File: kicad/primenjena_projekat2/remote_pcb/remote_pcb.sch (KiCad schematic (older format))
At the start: 24 parts, among them J1 BATT_9V, J2 UART1, J3 ICSP, P1 joystick, SW1 SW_RST, U1 L7805, U2 DSPIC30f4013, Y1 Crystal

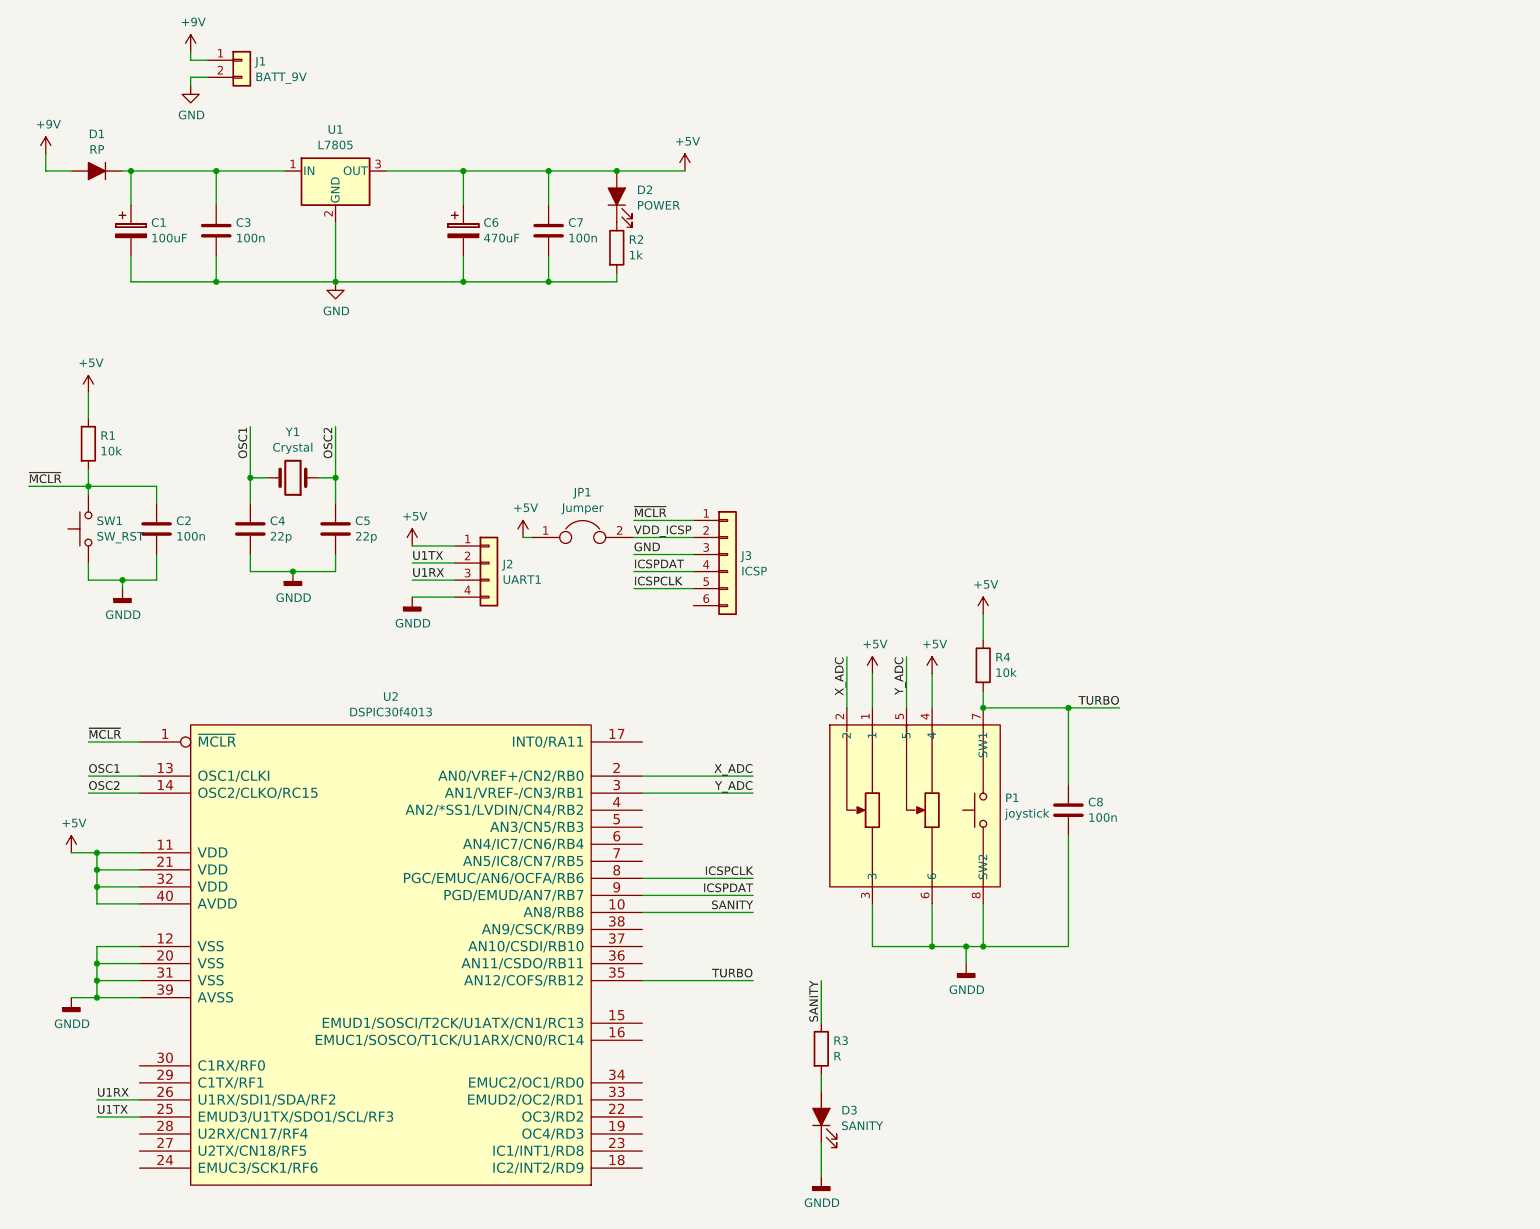
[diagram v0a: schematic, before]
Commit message: Remote control PCB
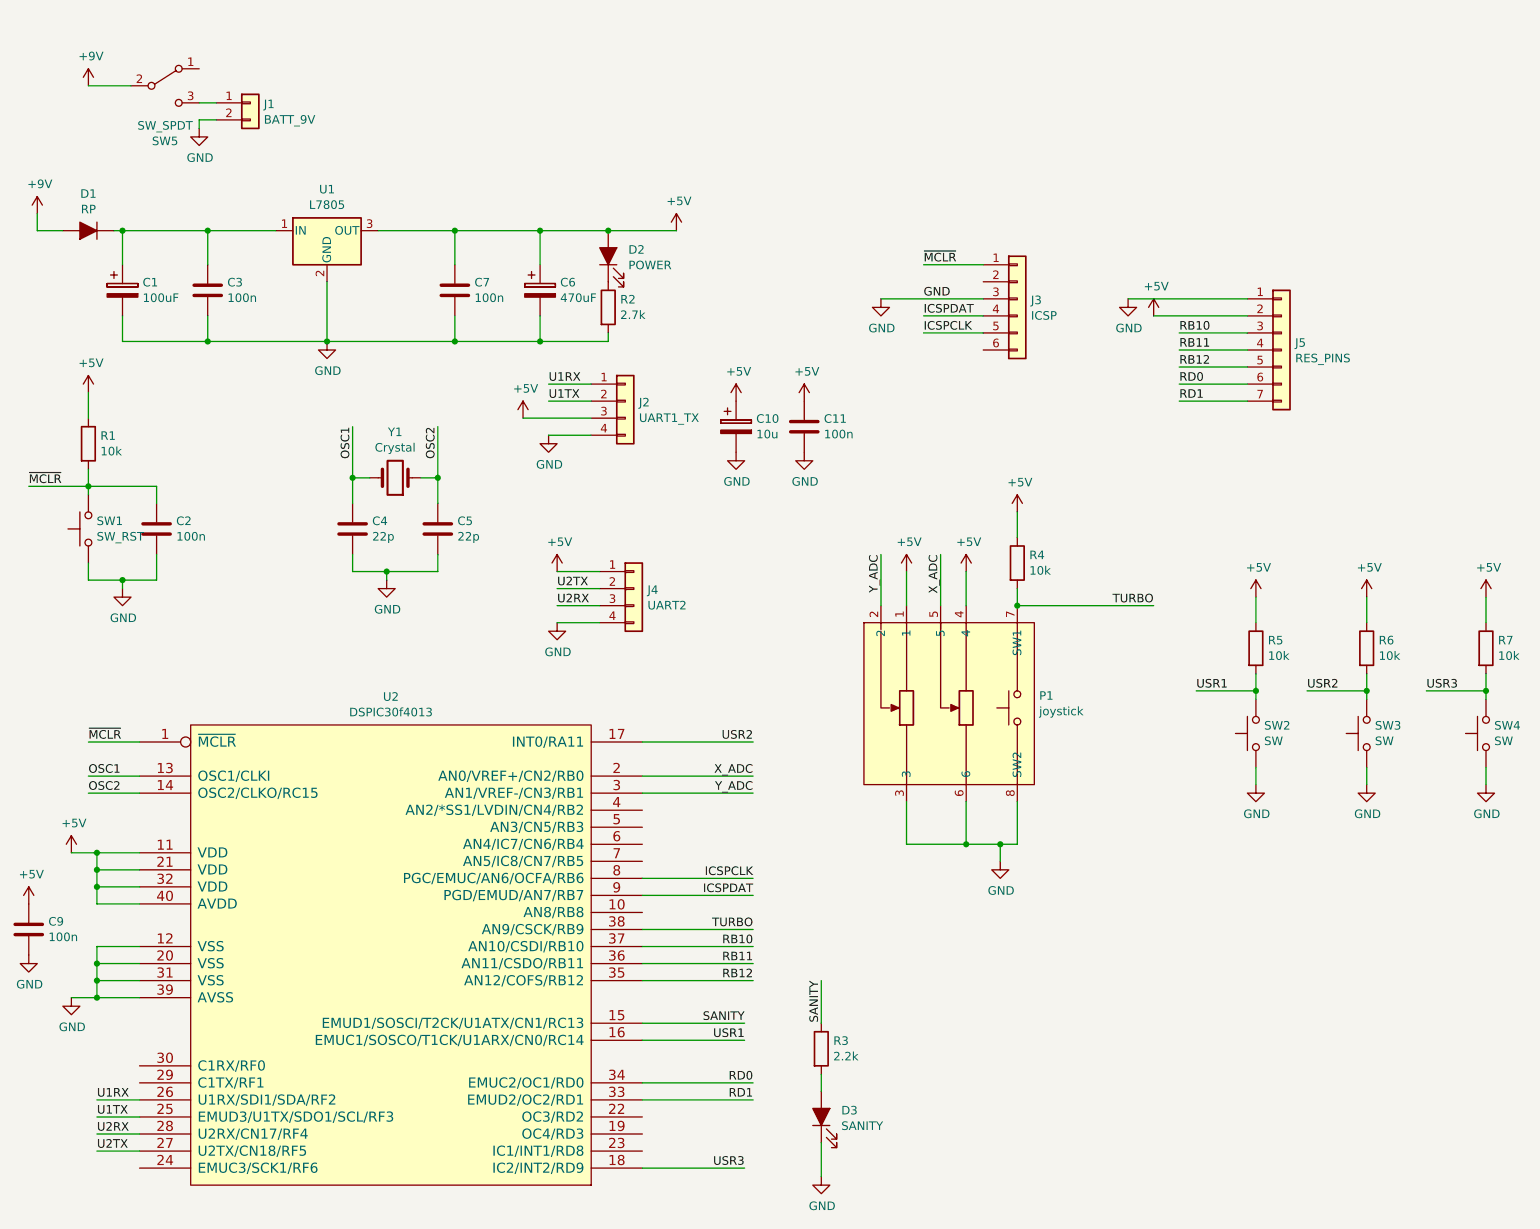
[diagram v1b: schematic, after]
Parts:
- removed C8: 100n, symbol Device:C
- removed JP1: Jumper, symbol Device:Jumper
- added C10: 10u, Capacitor_THT:CP_Radial_D5.0mm_P2.50mm, symbol Device:CP
- added C11, C9: 100n, Capacitor_THT:C_Disc_D5.0mm_W2.5mm_P2.50mm, symbol Device:C
- added J4: UART2, Connector_PinHeader_2.54mm:PinHeader_1x04_P2.54mm_Vertical, symbol Connector_Generic:Conn_01x04
- added J5: RES_PINS, Connector_PinHeader_2.54mm:PinHeader_1x07_P2.54mm_Vertical, symbol Connector_Generic:Conn_01x07
- added R5, R6, R7: 10k, Resistor_THT:R_Axial_DIN0207_L6.3mm_D2.5mm_P10.16mm_Horizontal, symbol Device:R
- added SW2, SW3, SW4: SW, Button_Switch_THT:SW_PUSH_6mm, symbol Switch:SW_Push
- added SW5: SW_SPDT, TerminalBlock_RND:TerminalBlock_RND_205-00068_1x03_P7.50mm_Horizontal, symbol Switch:SW_SPDT
- C1, C6: footprint (none) -> Capacitor_THT:CP_Radial_D7.5mm_P2.50mm
- C2, C3, C4, C5, C7: footprint (none) -> Capacitor_THT:C_Disc_D5.0mm_W2.5mm_P2.50mm
- D1: footprint (none) -> Diode_THT:D_DO-34_SOD68_P7.62mm_Horizontal
- D2, D3: footprint (none) -> LED_THT:LED_D5.0mm
- J1: footprint (none) -> TerminalBlock:TerminalBlock_Altech_AK300-2_P5.00mm
- J2: value UART1 -> UART1_TX; footprint (none) -> Connector_PinHeader_2.54mm:PinHeader_1x04_P2.54mm_Vertical
- J3: footprint (none) -> Connector_PinHeader_2.54mm:PinHeader_1x06_P2.54mm_Vertical
- P1: footprint (none) -> footprints:joystick
- R1, R4: footprint (none) -> Resistor_THT:R_Axial_DIN0207_L6.3mm_D2.5mm_P10.16mm_Horizontal
- R2: value 1k -> 2.7k; footprint (none) -> Resistor_THT:R_Axial_DIN0207_L6.3mm_D2.5mm_P10.16mm_Horizontal
- R3: value R -> 2.2k; footprint (none) -> Resistor_THT:R_Axial_DIN0207_L6.3mm_D2.5mm_P10.16mm_Horizontal
- SW1: footprint (none) -> Button_Switch_THT:SW_PUSH_6mm
- U1: footprint (none) -> Package_TO_SOT_THT:TO-220-3_Vertical
- Y1: footprint (none) -> Crystal:Crystal_HC50_Vertical
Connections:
- net GNDD is gone; now on net GND: C2.2, C4.2, C5.2, D3.1 (K), J2.4 (Pin_4), P1.3, P1.6, P1.8 (SW2), SW1.1, U2.12 (VSS), U2.20 (VSS), U2.31 (VSS), U2.39 (AVSS)
- net +5V: now also J2.3 (Pin_3), C10.1, C11.1, C9.1, J4.1 (Pin_1), J5.2 (Pin_2), R5.1, R6.1, R7.1; no longer J2.1 (Pin_1)
- net +9V: now also SW5.2 (B); no longer J1.1 (Pin_1)
- net GND: now also C10.2, C11.2, C9.2, J4.4 (Pin_4), J5.1 (Pin_1), SW2.1, SW3.1, SW4.1
- net SANITY: now also U2.15 (EMUD1/SOSCI/T2CK/U1ATX/CN1/RC13); no longer U2.10 (AN8/RB8)
- net TURBO: now also U2.38 (AN9/CSCK/RB9); no longer U2.35 (AN12/COFS/RB12)
- net U1RX: now also J2.1 (Pin_1); no longer J2.3 (Pin_3)
- net X_ADC: now also P1.5; no longer P1.2
- net Y_ADC: now also P1.2; no longer P1.5
- net USR1: now reaches U2.16 (EMUC1/SOSCO/T1CK/U1ARX/CN0/RC14)
- net USR1: now also R5.2, SW2.2
- net USR2: now reaches U2.17 (INT0/RA11)
- net USR2: now also R6.2, SW3.2
- net USR3: now reaches U2.18 (IC2/INT2/RD9)
- net USR3: now also R7.2, SW4.2
- net U2TX: now reaches U2.27 (U2TX/CN18/RF5)
- net U2TX: now also J4.2 (Pin_2)
- net U2RX: now reaches U2.28 (U2RX/CN17/RF4)
- net U2RX: now also J4.3 (Pin_3)
- net RD1: now reaches U2.33 (EMUD2/OC2/RD1)
- net RD1: now also J5.7 (Pin_7)
- net RD0: now reaches U2.34 (EMUC2/OC1/RD0)
- net RD0: now also J5.6 (Pin_6)
- net RB11: now reaches U2.36 (AN11/CSDO/RB11)
- net RB11: now also J5.4 (Pin_4)
- net RB10: now reaches U2.37 (AN10/CSDI/RB10)
- net RB10: now also J5.3 (Pin_3)
- net VDD_ICSP: no longer names the net of J3.2 (Pin_2)
- new net: J1.1 (Pin_1), SW5.3 (C)
- new net RB12: J5.5 (Pin_5), U2.35 (AN12/COFS/RB12)
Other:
- moved on the sheet: C1, C3, C4, C5, C6, C7, D1, D2, J1, J2, J3, P1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
